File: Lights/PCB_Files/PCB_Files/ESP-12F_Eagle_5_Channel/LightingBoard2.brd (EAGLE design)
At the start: 53 x 35.5 mm, 37 parts, among them Q1 A2SHB, Q2 A2SHB, Q3 A2SHB, Q4 A2SHB, Q5 A2SHB

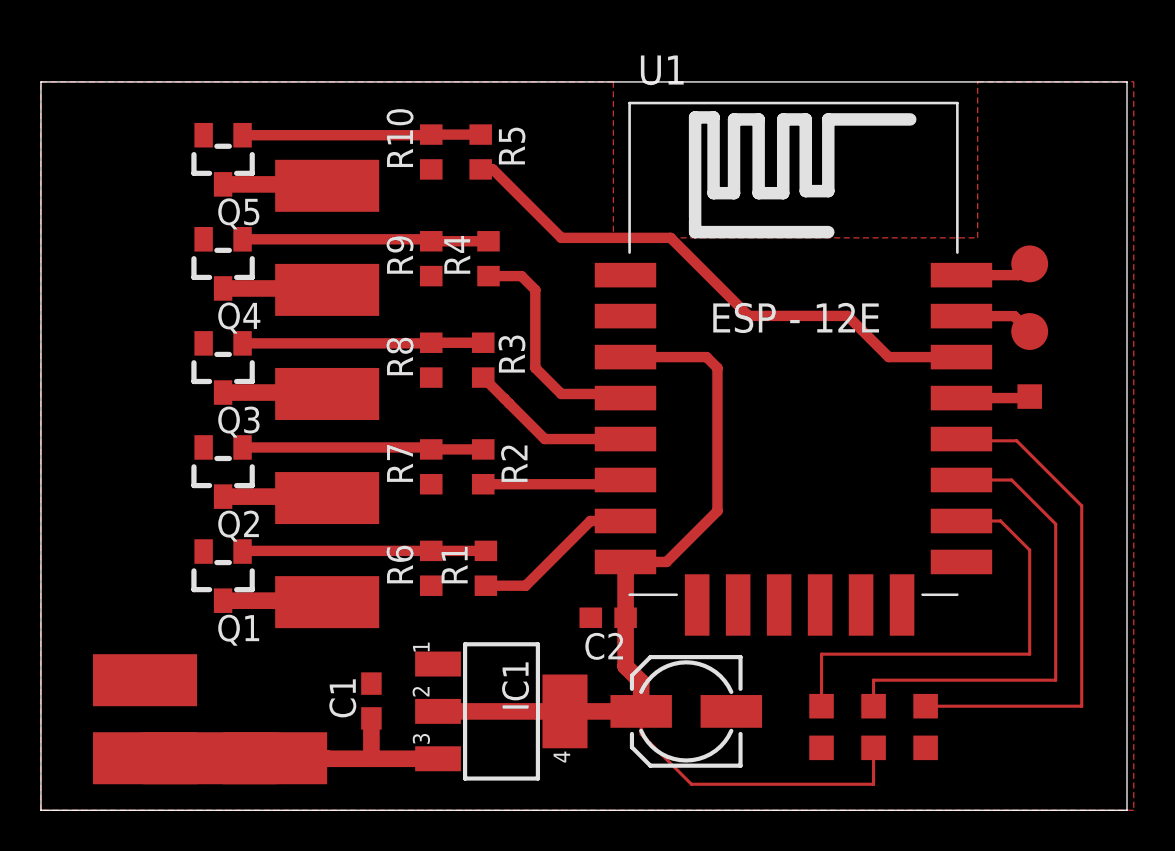
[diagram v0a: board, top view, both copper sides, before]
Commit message: Increased thickness of undersized tracks
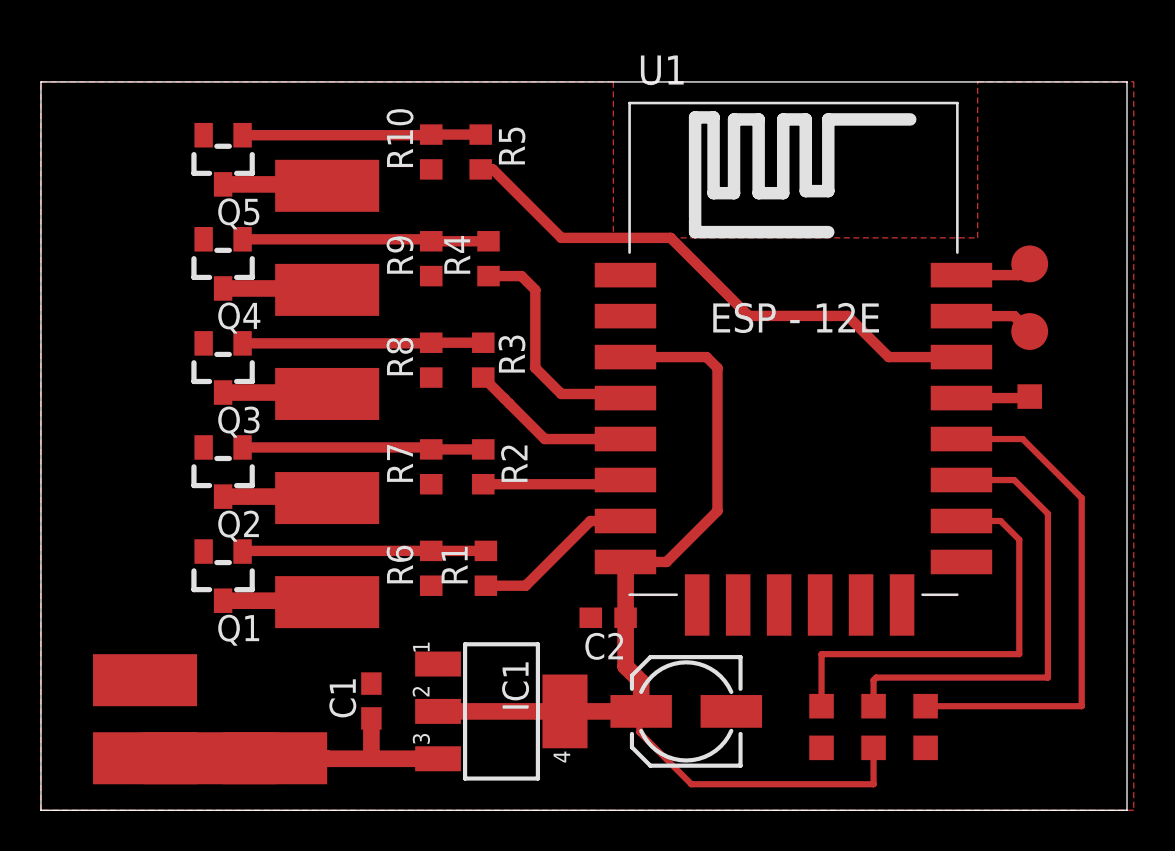
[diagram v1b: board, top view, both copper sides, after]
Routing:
- net N$23: track 21.7 -> 21.0 mm
- net N$24: track 23.3 -> 22.7 mm
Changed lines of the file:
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@@
 <contactref element="C2" pad="1"/>
 <contactref element="C3" pad="+"/>
-<wire x1="19.3802" y1="4.826" x2="29.296" y2="4.826" width="0.8128" layer="1"/>
+<wire x1="19.3802" y1="4.826" x2="29.21" y2="4.826" width="0.8128" layer="1"/>
+<wire x1="29.21" y1="4.826" x2="29.296" y2="4.826" width="0.8128" layer="1"/>
 <wire x1="29.296" y1="4.826" x2="29.296" y2="6.264" width="0.8128" layer="1"/>
 <wire x1="29.296" y1="6.264" x2="28.536" y2="7.024" width="0.8128" layer="1"/>
 <wire x1="28.536" y1="7.024" x2="28.536" y2="9.398" width="0.8128" layer="1"/>
-<wire x1="40.64" y1="3.048" x2="40.64" y2="1.27" width="0.1524" layer="1"/>
-<wire x1="40.64" y1="1.27" x2="31.75" y2="1.27" width="0.1524" layer="1"/>
-<wire x1="29.296" y1="3.724" x2="29.296" y2="4.826" width="0.1524" layer="1"/>
-<wire x1="31.75" y1="1.27" x2="29.296" y2="3.724" width="0.1524" layer="1"/>
 <wire x1="28.53" y1="12.12" x2="30.535" y2="12.12" width="0.508" layer="1"/>
 <wire x1="30.535" y1="12.12" x2="33.02" y2="14.605" width="0.508" layer="1"/>
@@
 <wire x1="28.536" y1="9.398" x2="28.536" y2="12.114" width="0.8128" layer="1"/>
 <wire x1="28.536" y1="12.114" x2="28.53" y2="12.12" width="0.8128" layer="1"/>
+<wire x1="40.64" y1="3.048" x2="40.64" y2="1.27" width="0.3048" layer="1"/>
+<wire x1="40.64" y1="1.27" x2="31.75" y2="1.27" width="0.3048" layer="1"/>
+<wire x1="31.75" y1="1.27" x2="29.21" y2="3.81" width="0.3048" layer="1"/>
+<wire x1="29.21" y1="3.81" x2="29.21" y2="4.826" width="0.3048" layer="1"/>
 </signal>
 <signal name="N$21">
@@
 <contactref element="U1" pad="GPIO15"/>
 <contactref element="TP3" pad="TP"/>
-<wire x1="44.93" y1="14.12" x2="46.84" y2="14.12" width="0.1524" layer="1"/>
-<wire x1="46.84" y1="14.12" x2="48.26" y2="12.7" width="0.1524" layer="1"/>
-<wire x1="48.26" y1="12.7" x2="48.26" y2="7.62" width="0.1524" layer="1"/>
-<wire x1="48.26" y1="7.62" x2="38.1" y2="7.62" width="0.1524" layer="1"/>
-<wire x1="38.1" y1="7.62" x2="38.1" y2="5.08" width="0.1524" layer="1"/>
+<wire x1="38.1" y1="5.08" x2="38.1" y2="7.62" width="0.3048" layer="1"/>
+<wire x1="38.1" y1="7.62" x2="47.752" y2="7.62" width="0.3048" layer="1"/>
+<wire x1="47.752" y1="7.62" x2="47.752" y2="13.208" width="0.3048" layer="1"/>
+<wire x1="46.84" y1="14.12" x2="44.93" y2="14.12" width="0.3048" layer="1"/>
+<wire x1="47.752" y1="13.208" x2="46.84" y2="14.12" width="0.3048" layer="1"/>
 </signal>
 <signal name="N$24">
 <contactref element="U1" pad="GPIO2"/>
 <contactref element="TP4" pad="TP"/>
-<wire x1="40.64" y1="5.08" x2="40.64" y2="6.35" width="0.1524" layer="1"/>
-<wire x1="40.64" y1="6.35" x2="49.53" y2="6.35" width="0.1524" layer="1"/>
-<wire x1="49.53" y1="6.35" x2="49.53" y2="13.97" width="0.1524" layer="1"/>
-<wire x1="49.53" y1="13.97" x2="47.38" y2="16.12" width="0.1524" layer="1"/>
-<wire x1="47.38" y1="16.12" x2="44.93" y2="16.12" width="0.1524" layer="1"/>
+<wire x1="40.64" y1="5.08" x2="40.64" y2="6.35" width="0.3048" layer="1"/>
+<wire x1="40.64" y1="6.35" x2="40.767" y2="6.477" width="0.3048" layer="1"/>
+<wire x1="40.767" y1="6.477" x2="49.149" y2="6.477" width="0.3048" layer="1"/>
+<wire x1="49.149" y1="6.477" x2="49.149" y2="14.478" width="0.3048" layer="1"/>
+<wire x1="47.507" y1="16.12" x2="44.93" y2="16.12" width="0.3048" layer="1"/>
+<wire x1="49.149" y1="14.478" x2="47.507" y2="16.12" width="0.3048" layer="1"/>
 </signal>
 <signal name="N$25">
 <contactref element="U1" pad="GPIO0"/>
 <contactref element="TP5" pad="TP"/>
-<wire x1="44.93" y1="18.12" x2="45.016" y2="18.034" width="0.3048" layer="1"/>
-<wire x1="45.016" y1="18.034" x2="47.625" y2="18.034" width="0.1524" layer="1"/>
-<wire x1="47.625" y1="18.034" x2="50.8" y2="14.859" width="0.1524" layer="1"/>
-<wire x1="50.8" y1="14.859" x2="50.8" y2="5.08" width="0.1524" layer="1"/>
-<wire x1="50.8" y1="5.08" x2="43.18" y2="5.08" width="0.1524" layer="1"/>
+<wire x1="44.93" y1="18.12" x2="47.92" y2="18.12" width="0.3048" layer="1"/>
+<wire x1="47.92" y1="18.12" x2="50.8" y2="15.24" width="0.3048" layer="1"/>
+<wire x1="50.8" y1="15.24" x2="50.8" y2="5.08" width="0.3048" layer="1"/>
+<wire x1="50.8" y1="5.08" x2="43.18" y2="5.08" width="0.3048" layer="1"/>
 </signal>
 <signal name="N$6">
